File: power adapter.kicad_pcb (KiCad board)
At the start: 2 copper layers, 63.5 x 38.1 mm, 6 parts

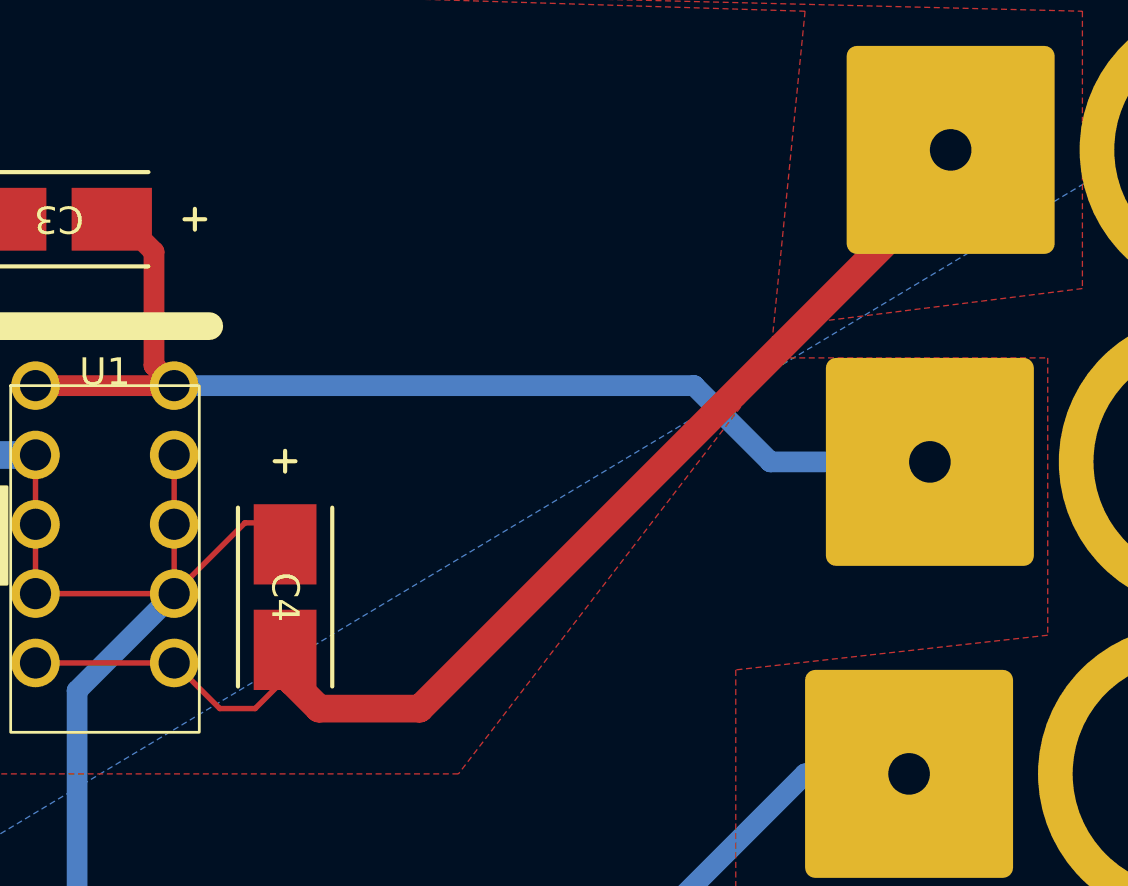
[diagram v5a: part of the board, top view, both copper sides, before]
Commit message: traces to cap
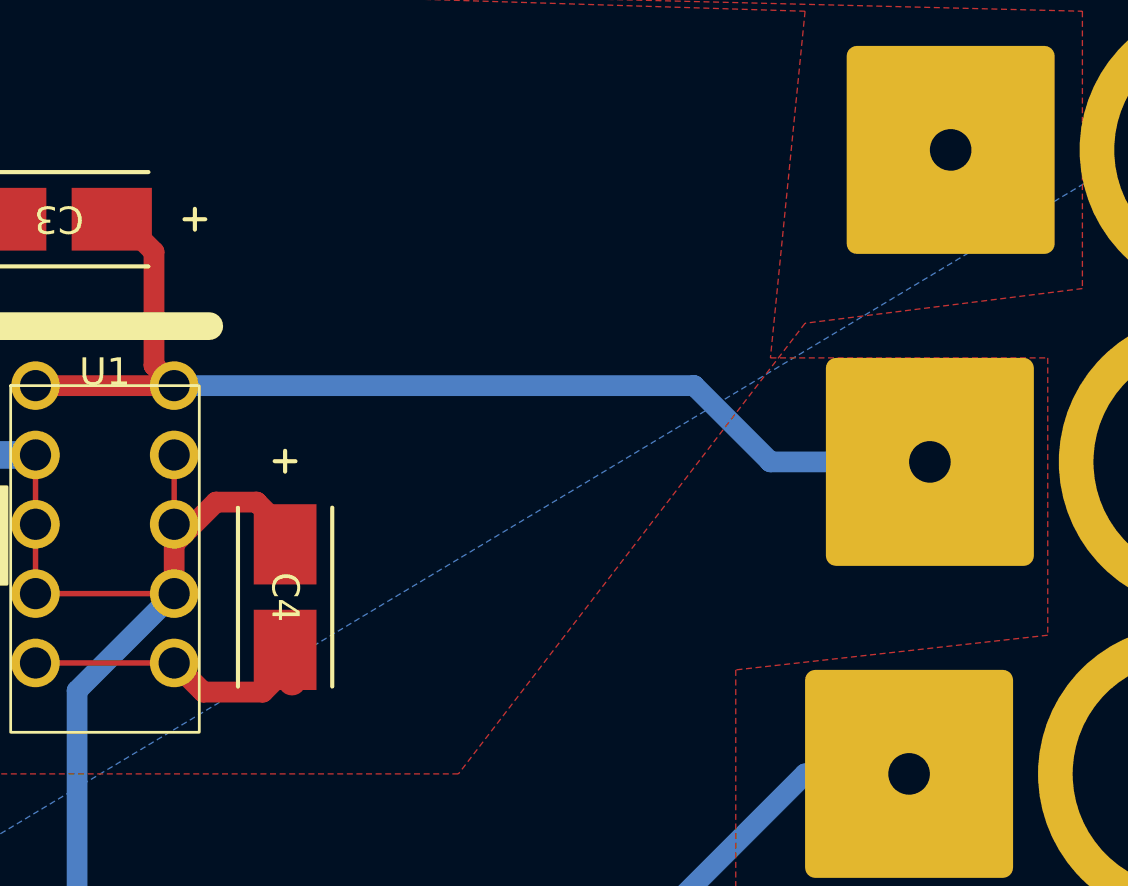
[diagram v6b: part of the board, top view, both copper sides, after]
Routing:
- net -12V: track 45.3 -> 12.7 mm
- net GND: track 82.3 -> 85.5 mm
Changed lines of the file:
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@@
+	)
+	(segment
+		(start 45.947018 95.452806)
+		(end 44.456088 95.452806)
+		(width 0.762)
+		(layer "F.Cu")
+		(net 1)
+	)
+	(segment
+		(start 42.926 96.982894)
+		(end 42.926 98.806)
+		(width 0.762)
+		(layer "F.Cu")
+		(net 1)
 	)
 	(segment
@@
 	)
 	(segment
-		(start 45.51849 96.21351)
-		(end 46.084624 96.21351)
-		(width 0.2)
+		(start 46.99 96.495788)
+		(end 45.947018 95.452806)
+		(width 0.762)
+		(layer "F.Cu")
+		(net 1)
+	)
+	(segment
+		(start 44.456088 95.452806)
+		(end 42.926 96.982894)
+		(width 0.762)
+		(layer "F.Cu")
+		(net 1)
+	)
+	(segment
+		(start 46.99 96.999704)
+		(end 46.99 96.495788)
+		(width 0.762)
 		(layer "F.Cu")
 		(net 1)
@@
 		(end 36.089886 85.09)
 		(width 1.016)
-		(layer "F.Cu")
-		(net 1)
-	)
-	(segment
-		(start 42.926 98.806)
-		(end 45.51849 96.21351)
-		(width 0.2)
 		(layer "F.Cu")
 		(net 1)
@@
 	)
 	(segment
-		(start 48.234376 103.019898)
-		(end 47.244 102.029522)
-		(width 1.016)
-		(layer "F.Cu")
-		(net 2)
-	)
-	(segment
-		(start 42.926 101.346)
-		(end 44.596698 103.016698)
-		(width 0.2)
-		(layer "F.Cu")
-		(net 2)
-	)
-	(segment
-		(start 45.894003 103.016698)
-		(end 47.244 101.666701)
-		(width 0.2)
+		(start 43.993194 102.413194)
+		(end 46.176806 102.413194)
+		(width 0.762)
+		(layer "F.Cu")
+		(net 2)
+	)
+	(segment
+		(start 46.176806 102.413194)
+		(end 46.99 101.6)
+		(width 0.762)
 		(layer "F.Cu")
 		(net 2)
@@
 	)
 	(segment
-		(start 51.920102 103.019898)
-		(end 48.234376 103.019898)
-		(width 1.016)
+		(start 42.926 101.346)
+		(end 43.993194 102.413194)
+		(width 0.762)
 		(layer "F.Cu")
 		(net 2)
@@
 	)
 	(segment
-		(start 71.374 83.566)
-		(end 51.920102 103.019898)
-		(width 1.016)
-		(layer "F.Cu")
-		(net 2)
-	)
-	(segment
-		(start 44.596698 103.016698)
-		(end 45.894003 103.016698)
-		(width 0.2)
-		(layer "F.Cu")
-		(net 2)
+		(start 46.99 101.6)
+		(end 46.99 100.866296)
+		(width 0.762)
+		(layer "F.Cu")
+		(net 2)

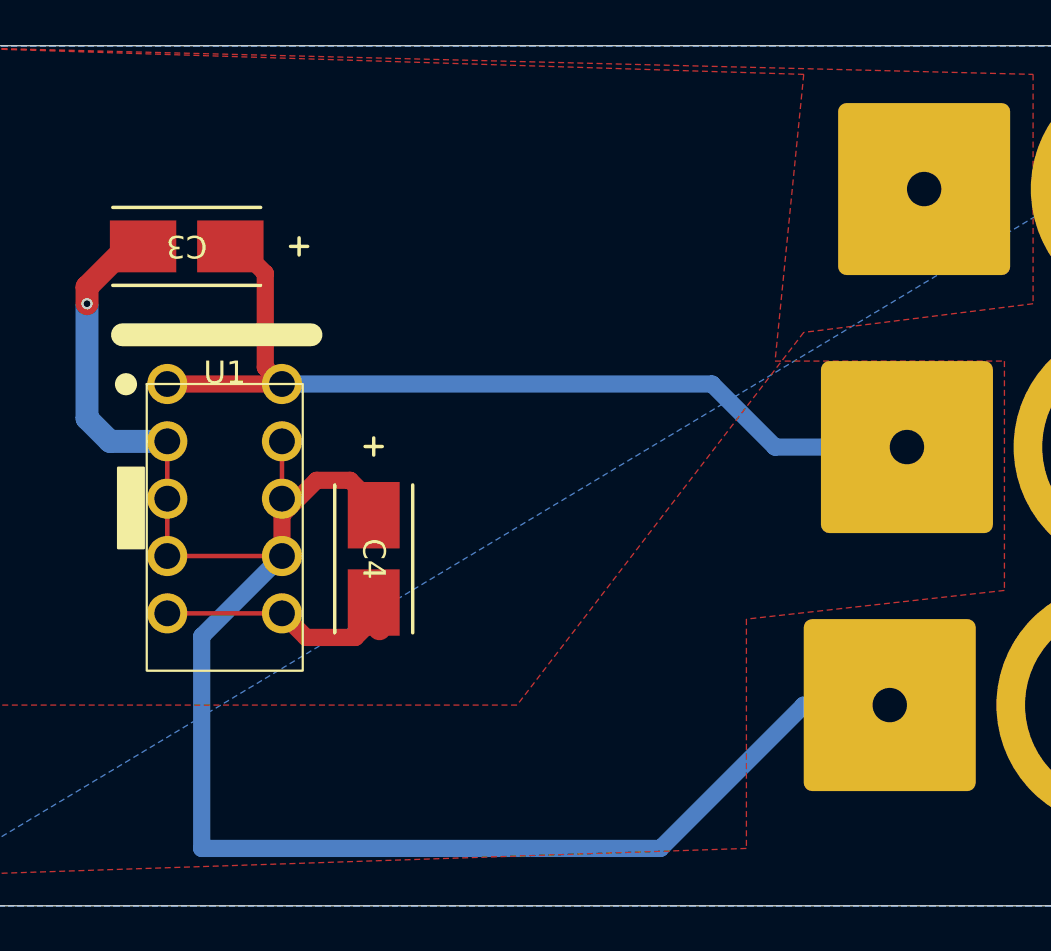
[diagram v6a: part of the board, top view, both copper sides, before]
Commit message: added ceramic caps
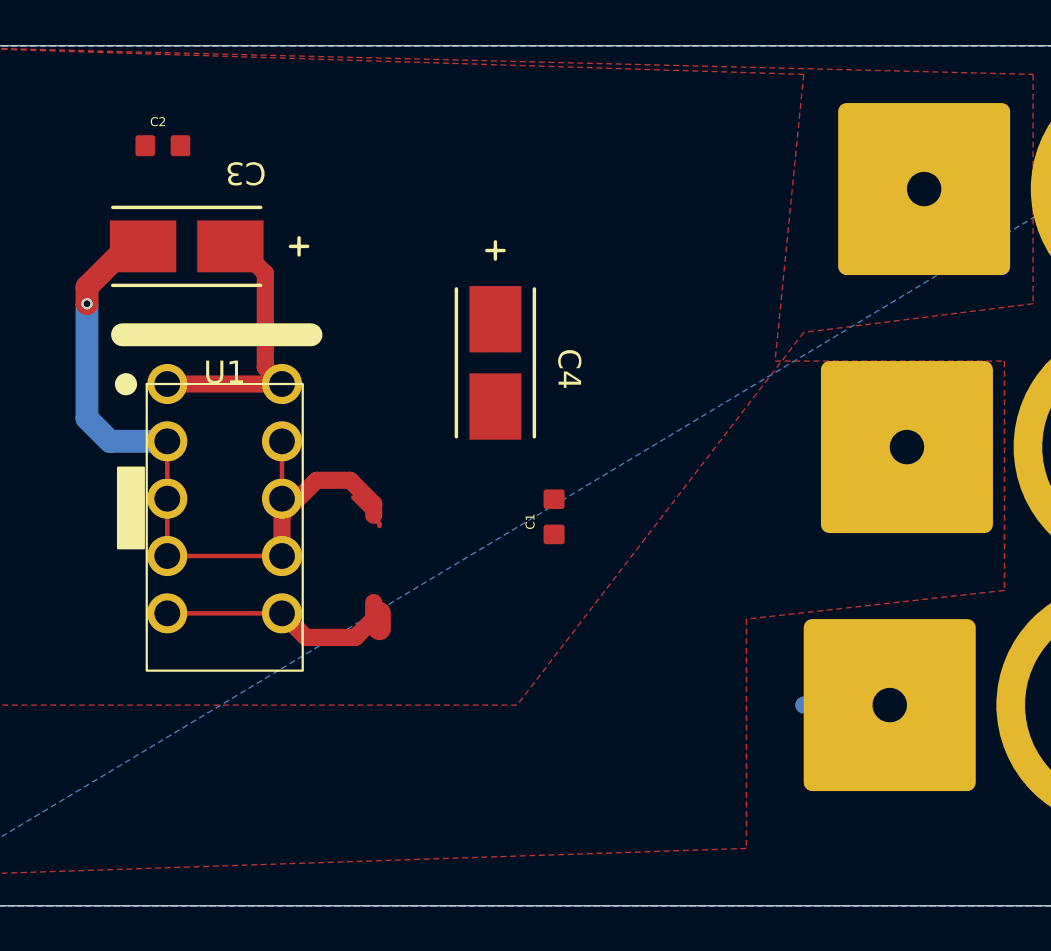
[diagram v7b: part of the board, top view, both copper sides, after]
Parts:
- added C1: .1uF, adpterpcblib:CAPC1608X90N, F.Cu at (55.0, 97.1)
- added C2: .01uF, adpterpcblib:CAPC1608X90N, F.Cu at (37.6, 80.6)
- moved C4 10.2 mm to (52.4, 90.2)
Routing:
- net GND: track 85.5 -> 41.8 mm
- net +12V: track 41.3 -> 12.4 mm

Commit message: fixedc2
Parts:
- moved C4 10.4 mm to (47.6, 99.5)
- moved C1 3.92 mm to (52.3, 99.9)
- moved C2 3.52 mm to (41.1, 81.4), turned to 180 degrees
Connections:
- C2 pad 1: GND -> +12V
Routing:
- net GND: track 41.8 -> 55.3 mm
- net +12V: track 12.4 -> 17.0 mm
